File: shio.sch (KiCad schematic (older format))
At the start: 82 parts, among them J1 10118193-0001LF, U1 LM66100DCKT, U2 MAX38640AENT+, U3 NRF52840-CKAA-R7, U4 LM66100DCKT, U5 BMA400, U6 W25N01GVZEIG_TR, U8 SiP32431DR3, Y1 32.768kHz, Y3 32MHz

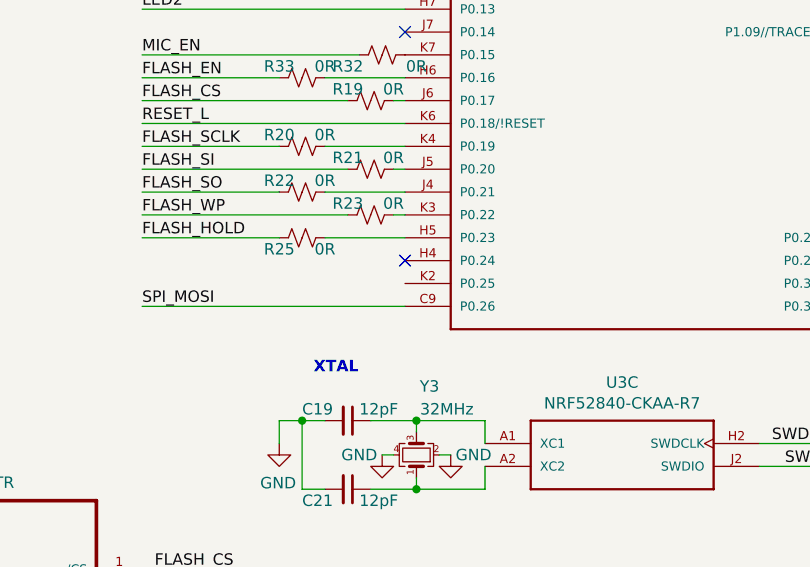
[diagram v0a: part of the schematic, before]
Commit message: Added modifications to stiffener instructions on eco layers
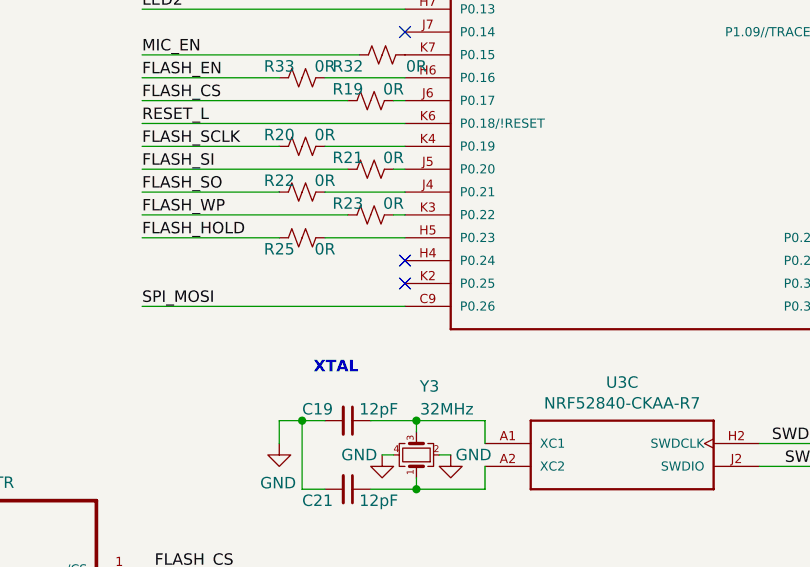
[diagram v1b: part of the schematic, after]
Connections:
- no-connect marks 25 -> 26
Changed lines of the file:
@@
 Wire Wire Line
 	9750 4300 10900 4300
+NoConn ~ 7550 5600
 $EndSCHEMATC

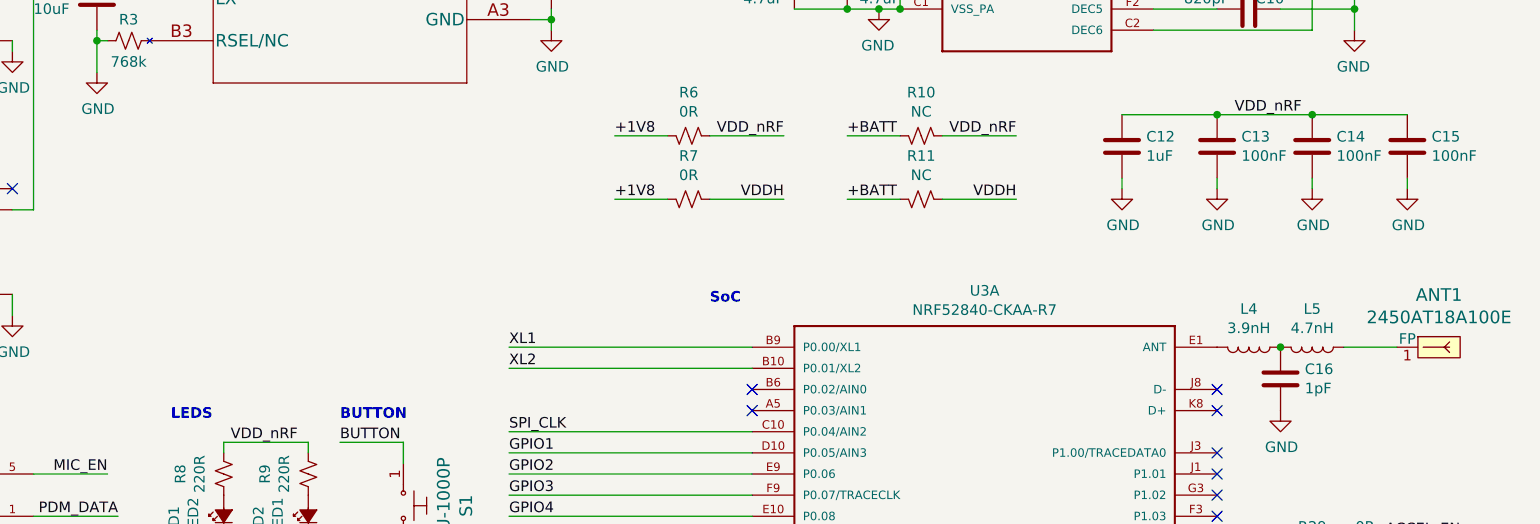
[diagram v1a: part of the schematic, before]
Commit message: New antenna components
- Added filter circuit for antenna
- Added extra test point for external UFL connector compatibility
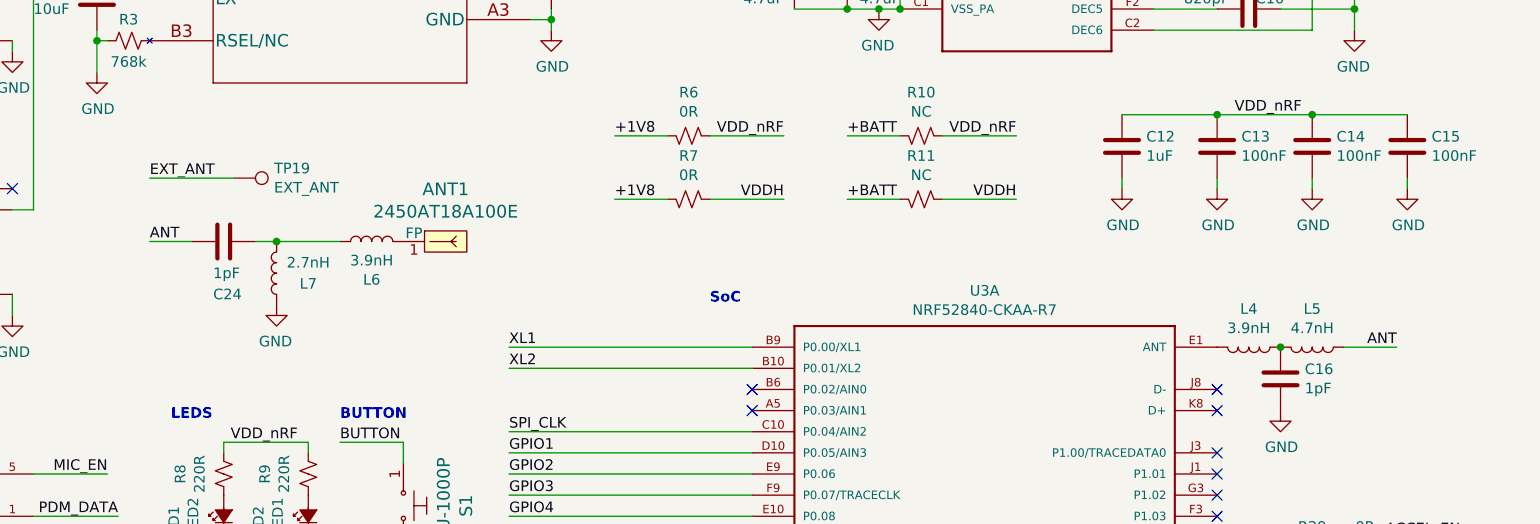
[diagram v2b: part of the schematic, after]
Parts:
- added C24: 1pF, Capacitor_SMD:C_0201_0603Metric, symbol Device:C
- added L6: 3.9nH, Inductor_SMD:L_0201_0603Metric, symbol Device:L
- added L7: 2.7nH, Inductor_SMD:L_0201_0603Metric, symbol Device:L
- added TP19: EXT_ANT, TestPoint:TestPoint_Pad_1.0x1.0mm, symbol Connector:TestPoint
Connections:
- net GND: now also L7.1
- net at ANT1.1 (FP): now also L6.2; no longer L5.1
- new net: C24.1, L6.1, L7.2
- new net ANT: C24.2, L5.1
- new net EXT_ANT: TP19.1
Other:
- moved on the sheet: ANT1
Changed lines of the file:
@@
 Text Label 8800 2400 2    50   ~ 0
 VDDH
-$Comp
-L dk_RF-Antennas:2450AT18A100E ANT1
-U 1 1 5FA64328
-P 10800 3100
-F 0 "ANT1" H 10800 3347 60  0000 C CNN
-F 1 "2450AT18A100E" H 10800 3241 60  0000 C CNN
-F 2 "digikey-footprints:Antenna_1.6x3.2mm_2450AT18A100E" H 11000 3300 60  0001 L CNN
-F 3 "https://www.johansontechnology.com/datasheets/2450AT18A100/2450AT18A100.pdf" H 11000 3400 60  0001 L CNN
-F 4 "712-1005-1-ND" H 11000 3500 60  0001 L CNN "Digi-Key_PN"
-F 5 "2450AT18A100E" H 11000 3600 60  0001 L CNN "MPN"
-F 6 "RF/IF and RFID" H 11000 3700 60  0001 L CNN "Category"
-F 7 "RF Antennas" H 11000 3800 60  0001 L CNN "Family"
-F 8 "https://www.johansontechnology.com/datasheets/2450AT18A100/2450AT18A100.pdf" H 11000 3900 60  0001 L CNN "DK_Datasheet_Link"
-F 9 "/product-detail/en/johanson-technology-inc/2450AT18A100E/712-1005-1-ND/1560834" H 11000 4000 60  0001 L CNN "DK_Detail_Page"
-F 10 "RF ANT 2.4GHZ CHIP SOLDER SMD" H 11000 4100 60  0001 L CNN "Description"
-F 11 "Johanson Technology Inc." H 11000 4200 60  0001 L CNN "Manufacturer"
-F 12 "Active" H 11000 4300 60  0001 L CNN "Status"
-	1    10800 3100
-	1    0    0    -1
-$EndComp
 Text Label 10850 5400 2    50   ~ 0
 SPI_CS
@@
 VDDH
 Wire Wire Line
-	5450 5450 5100 5450
-Wire Wire Line
-	5450 5350 5100 5350
-Wire Wire Line
-	5450 5250 5100 5250
-Wire Wire Line
-	5450 5050 5100 5050
-Wire Wire Line
-	3900 5350 3450 5350
-Wire Wire Line
-	3900 5250 3450 5250
-Text Label 3350 4750 0    50   ~ 0
-ACCEL_EN
-Connection ~ 3900 4750
-Wire Wire Line
-	3900 4850 3900 4750
-Connection ~ 3850 5750
-Wire Wire Line
-	3850 5650 3900 5650
-Wire Wire Line
-	3850 5750 3850 5650
-Wire Wire Line
-	3850 5750 3900 5750
-Wire Wire Line
-	3850 5800 3850 5750
-$Comp
-L power:GND #PWR023
-U 1 1 5EF0819A
-P 3850 5800
-F 0 "#PWR023" H 3850 5550 50  0001 C CNN
-F 1 "GND" H 3855 5627 50  0000 C CNN
-F 2 "" H 3850 5800 50  0001 C CNN
-F 3 "" H 3850 5800 50  0001 C CNN
-	1    3850 5800
-	-1   0    0    -1
-$EndComp
-Text Label 3450 5350 0    50   ~ 0
-ACCEL_INT2
-Text Label 3450 5250 0    50   ~ 0
-ACCEL_INT1
-Text Label 5450 5050 2    50   ~ 0
-SPI_CS
-Text Label 5450 5450 2    50   ~ 0
-SPI_MISO
-Text Label 5450 5350 2    50   ~ 0
-SPI_MOSI
-Text Label 5450 5250 2    50   ~ 0
-SPI_CLK
-$Comp
-L BMA400:BMA400 U5
-U 1 1 5EC56C4B
-P 4500 5250
-F 0 "U5" H 4500 6017 50  0000 C CNN
-F 1 "BMA400" H 4500 5926 50  0000 C CNN
-F 2 "Shio:XDCR_BMA400" H 4500 5250 50  0001 L BNN
-F 3 "BMA400" H 4500 5250 50  0001 L BNN
-F 4 "LGA-12 Bosch Tools" H 4500 5250 50  0001 L BNN "Field4"
-F 5 "Bosch Sensortec" H 4500 5250 50  0001 L BNN "Field5"
-F 6 "None" H 4500 5250 50  0001 L BNN "Field6"
-F 7 "Unavailable" H 4500 5250 50  0001 L BNN "Field7"
-F 8 "Accelerometer X, Y, Z Axis ±2g, 4g, 8g, 16g 12-LGA _2x2_" H 4500 5250 50  0001 L BNN "Field8"
-	1    4500 5250
-	-1   0    0    -1
-$EndComp
-Wire Wire Line
 	10200 750  10200 1400
 Connection ~ 10200 750
@@
 Wire Wire Line
 	800  6600 1350 6600
-$Comp
-L Device:C C23
-U 1 1 5F0263EE
-P 3750 4900
-F 0 "C23" H 3865 4946 50  0000 L CNN
-F 1 "100nF" H 3865 4855 50  0000 L CNN
-F 2 "Capacitor_SMD:C_0201_0603Metric" H 3788 4750 50  0001 C CNN
-F 3 "~" H 3750 4900 50  0001 C CNN
-	1    3750 4900
-	-1   0    0    -1
-$EndComp
-Wire Wire Line
-	3900 4750 3750 4750
-Connection ~ 3750 4750
-Wire Wire Line
-	3750 4750 3350 4750
-$Comp
-L power:GND #PWR0102
-U 1 1 5F03A122
-P 3750 5050
-F 0 "#PWR0102" H 3750 4800 50  0001 C CNN
-F 1 "GND" H 3600 5000 50  0000 C CNN
-F 2 "" H 3750 5050 50  0001 C CNN
-F 3 "" H 3750 5050 50  0001 C CNN
-	1    3750 5050
-	-1   0    0    -1
-$EndComp
 Wire Wire Line
 	800  6400 1350 6400
@@
 Text Notes 5600 3450 0    50   ~ 10
 BUTTON
-Text Notes 3350 4550 0    50   ~ 10
-ACCELEROMETER
 Text Notes 4800 6200 0    50   ~ 10
 FLASH
@@
 NoConn ~ 9750 4600
 $Comp
-L power:GND #PWR?
+L power:GND #PWR024
 U 1 1 5F2067A7
 P 10100 5500
-F 0 "#PWR?" H 10100 5250 50  0001 C CNN
+F 0 "#PWR024" H 10100 5250 50  0001 C CNN
 F 1 "GND" H 10105 5327 50  0000 C CNN
 F 2 "" H 10100 5500 50  0001 C CNN
@@
 	9750 4300 10900 4300
 NoConn ~ 7550 5600
+Text Label 10600 3100 2    50   ~ 0
+ANT
+$Comp
+L Device:C C24
+U 1 1 5EEC9FE3
+P 5050 2600
+F 0 "C24" V 5300 2550 50  0000 L CNN
+F 1 "1pF" V 5200 2550 50  0000 L CNN
+F 2 "Capacitor_SMD:C_0201_0603Metric" H 5088 2450 50  0001 C CNN
+F 3 "~" H 5050 2600 50  0001 C CNN
+	1    5050 2600
+	0    1    1    0
+$EndComp
+Text Label 4700 2600 0    50   ~ 0
+ANT
+Wire Wire Line
+	4700 2600 4900 2600
+$Comp
+L Connector:TestPoint TP19
+U 1 1 5EF8C668
+P 5100 2300
+F 0 "TP19" V 5054 2488 50  0000 L CNN
+F 1 "EXT_ANT" V 5145 2488 50  0000 L CNN
+F 2 "TestPoint:TestPoint_Pad_1.0x1.0mm" H 5300 2300 50  0001 C CNN
+F 3 "~" H 5300 2300 50  0001 C CNN
+	1    5100 2300
+	0    1    1    0
+$EndComp
+Wire Wire Line
+	4700 2300 5100 2300
+Text Label 4700 2300 0    50   ~ 0
+EXT_ANT
+Text Notes 3350 4550 0    50   ~ 10
+ACCELEROMETER
+$Comp
+L power:GND #PWR0102
+U 1 1 5F03A122
+P 3750 5050
+F 0 "#PWR0102" H 3750 4800 50  0001 C CNN
+F 1 "GND" H 3600 5000 50  0000 C CNN
+F 2 "" H 3750 5050 50  0001 C CNN
+F 3 "" H 3750 5050 50  0001 C CNN
+	1    3750 5050
+	-1   0    0    -1
+$EndComp
+Wire Wire Line
+	3750 4750 3350 4750
+Connection ~ 3750 4750
+Wire Wire Line
+	3900 4750 3750 4750
+$Comp
+L Device:C C23
+U 1 1 5F0263EE
+P 3750 4900
+F 0 "C23" H 3865 4946 50  0000 L CNN
+F 1 "100nF" H 3865 4855 50  0000 L CNN
+F 2 "Capacitor_SMD:C_0201_0603Metric" H 3788 4750 50  0001 C CNN
+F 3 "~" H 3750 4900 50  0001 C CNN
+	1    3750 4900
+	-1   0    0    -1
+$EndComp
+$Comp
+L BMA400:BMA400 U5
+U 1 1 5EC56C4B
+P 4500 5250
+F 0 "U5" H 4500 6017 50  0000 C CNN
+F 1 "BMA400" H 4500 5926 50  0000 C CNN
+F 2 "Shio:XDCR_BMA400" H 4500 5250 50  0001 L BNN
+F 3 "BMA400" H 4500 5250 50  0001 L BNN
+F 4 "LGA-12 Bosch Tools" H 4500 5250 50  0001 L BNN "Field4"
+F 5 "Bosch Sensortec" H 4500 5250 50  0001 L BNN "Field5"
+F 6 "None" H 4500 5250 50  0001 L BNN "Field6"
+F 7 "Unavailable" H 4500 5250 50  0001 L BNN "Field7"
+F 8 "Accelerometer X, Y, Z Axis ±2g, 4g, 8g, 16g 12-LGA _2x2_" H 4500 5250 50  0001 L BNN "Field8"
+	1    4500 5250
+	-1   0    0    -1
+$EndComp
+Text Label 5450 5250 2    50   ~ 0
+SPI_CLK
+Text Label 5450 5350 2    50   ~ 0
+SPI_MOSI
+Text Label 5450 5450 2    50   ~ 0
+SPI_MISO
+Text Label 5450 5050 2    50   ~ 0
+SPI_CS
+Text Label 3450 5250 0    50   ~ 0
+ACCEL_INT1
+Text Label 3450 5350 0    50   ~ 0
+ACCEL_INT2
+$Comp
+L power:GND #PWR023
+U 1 1 5EF0819A
+P 3850 5800
+F 0 "#PWR023" H 3850 5550 50  0001 C CNN
+F 1 "GND" H 3855 5627 50  0000 C CNN
+F 2 "" H 3850 5800 50  0001 C CNN
+F 3 "" H 3850 5800 50  0001 C CNN
+	1    3850 5800
+	-1   0    0    -1
+$EndComp
+Wire Wire Line
+	3850 5800 3850 5750
+Wire Wire Line
+	3850 5750 3900 5750
+Wire Wire Line
+	3850 5750 3850 5650
+Wire Wire Line
+	3850 5650 3900 5650
+Connection ~ 3850 5750
+Wire Wire Line
+	3900 4850 3900 4750
+Connection ~ 3900 4750
+Text Label 3350 4750 0    50   ~ 0
+ACCEL_EN
+Wire Wire Line
+	3900 5250 3450 5250
+Wire Wire Line
+	3900 5350 3450 5350
+Wire Wire Line
+	5450 5050 5100 5050
+Wire Wire Line
+	5450 5250 5100 5250
+Wire Wire Line
+	5450 5350 5100 5350
+Wire Wire Line
+	5450 5450 5100 5450
+$Comp
+L Device:L L6
+U 1 1 5EECA836
+P 5750 2600
+F 0 "L6" V 5569 2600 50  0000 C CNN
+F 1 "3.9nH" V 5660 2600 50  0000 C CNN
+F 2 "Inductor_SMD:L_0201_0603Metric" H 5750 2600 50  0001 C CNN
+F 3 "~" H 5750 2600 50  0001 C CNN
+	1    5750 2600
+	0    -1   -1   0
+$EndComp
+$Comp
+L dk_RF-Antennas:2450AT18A100E ANT1
+U 1 1 5FA64328
+P 6100 2600
+F 0 "ANT1" H 6100 2847 60  0000 C CNN
+F 1 "2450AT18A100E" H 6100 2741 60  0000 C CNN
+F 2 "digikey-footprints:Antenna_1.6x3.2mm_2450AT18A100E" H 6300 2800 60  0001 L CNN
+F 3 "https://www.johansontechnology.com/datasheets/2450AT18A100/2450AT18A100.pdf" H 6300 2900 60  0001 L CNN
+F 4 "712-1005-1-ND" H 6300 3000 60  0001 L CNN "Digi-Key_PN"
+F 5 "2450AT18A100E" H 6300 3100 60  0001 L CNN "MPN"
+F 6 "RF/IF and RFID" H 6300 3200 60  0001 L CNN "Category"
+F 7 "RF Antennas" H 6300 3300 60  0001 L CNN "Family"
+F 8 "https://www.johansontechnology.com/datasheets/2450AT18A100/2450AT18A100.pdf" H 6300 3400 60  0001 L CNN "DK_Datasheet_Link"
+F 9 "/product-detail/en/johanson-technology-inc/2450AT18A100E/712-1005-1-ND/1560834" H 6300 3500 60  0001 L CNN "DK_Detail_Page"
+F 10 "RF ANT 2.4GHZ CHIP SOLDER SMD" H 6300 3600 60  0001 L CNN "Description"
+F 11 "Johanson Technology Inc." H 6300 3700 60  0001 L CNN "Manufacturer"
+F 12 "Active" H 6300 3800 60  0001 L CNN "Status"
+	1    6100 2600
+	1    0    0    -1
+$EndComp
+Connection ~ 5300 2600
+Wire Wire Line
+	5300 2600 5600 2600
+Wire Wire Line
+	5200 2600 5300 2600
+$Comp
+L power:GND #PWR08
+U 1 1 5EF3F919
+P 5300 2900
+F 0 "#PWR08" H 5300 2650 50  0001 C CNN
+F 1 "GND" H 5305 2727 50  0000 C CNN
+F 2 "" H 5300 2900 50  0001 C CNN
+F 3 "" H 5300 2900 50  0001 C CNN
+	1    5300 2900
+	-1   0    0    -1
+$EndComp
+$Comp
+L Device:L L7
+U 1 1 5EECA3DD
+P 5300 2750
+F 0 "L7" H 5150 2800 50  0000 C CNN
+F 1 "2.7nH" H 5150 2700 50  0000 C CNN
+F 2 "Inductor_SMD:L_0201_0603Metric" H 5300 2750 50  0001 C CNN
+F 3 "~" H 5300 2750 50  0001 C CNN
+	1    5300 2750
+	-1   0    0    1
+$EndComp
 $EndSCHEMATC
